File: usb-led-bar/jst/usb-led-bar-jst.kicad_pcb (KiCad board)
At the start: 2 copper layers, 100 x 15 mm, 18 parts, among them J1 JST PH 2-pin

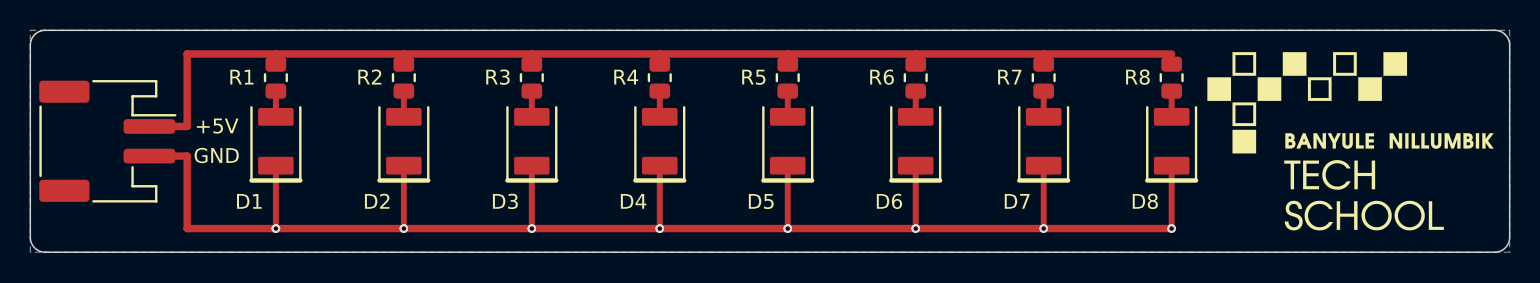
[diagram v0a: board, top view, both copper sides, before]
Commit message: Blank underside and M3 mounting hole at the logo end (both variants)
- Remove all back-side silkscreen (title, specs, JLC order-number marker);
  README now says to pick "Remove Mark" when ordering
- Add an M3 hole (3.2 mm NPTH, 6.9 mm head/washer keep-out) between D8
  and the logo; LED pitch 8.65 -> 7.65 mm to make room
- Regenerated schematics, boards (DRC clean, nets match), JLCPCB
  Gerber/BOM/CPL, previews and the USB-C STEP model; make_3d.py skips
  mounting-hole footprints

Co-Authored-By: Claude Opus 5.5 <noreply@anthropic.com>
Claude-Session: https://claude.ai/code/session_013C9F11DiXqXJzCTtebCnow
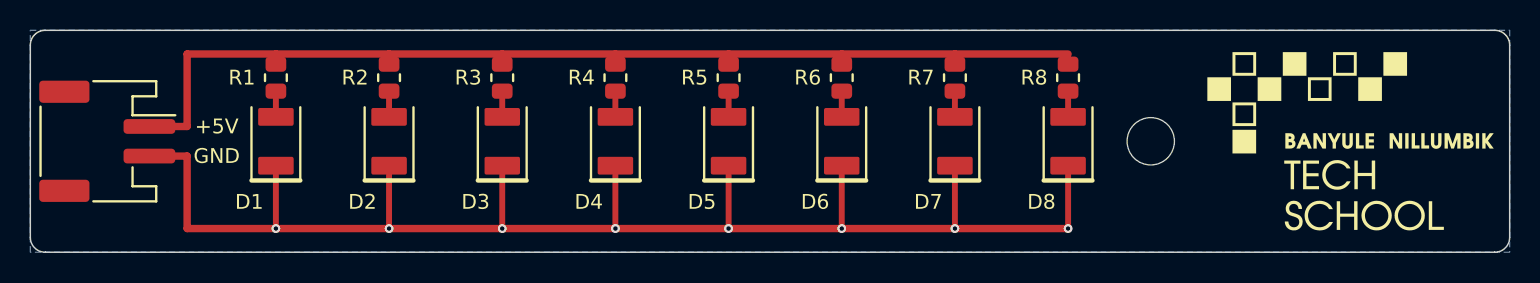
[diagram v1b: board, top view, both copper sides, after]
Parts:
- added H1: M3, MountingHole:MountingHole_3.2mm_M3, F.Cu at (175.7, 107.5)
- moved D8 7.00 mm to (170.2, 107.5)
- moved R8 7.00 mm to (170.2, 103.2)
- moved D7 6.00 mm to (162.5, 107.5)
- moved R7 6.00 mm to (162.5, 103.2)
- moved D6 5.00 mm to (154.8, 107.5)
- moved R6 5.00 mm to (154.8, 103.2)
- moved D5 4.00 mm to (147.2, 107.5)
- moved R5 4.00 mm to (147.2, 103.2)
- moved D4 3.00 mm to (139.6, 107.5)
- moved R4 3.00 mm to (139.6, 103.2)
- moved D3 2.00 mm to (131.9, 107.5)
- moved R3 2.00 mm to (131.9, 103.2)
- moved D2 1.00 mm to (124.2, 107.5)
- moved R2 1.00 mm to (124.2, 103.2)
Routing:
- net GND: track 108.0 -> 101.0 mm
- net +5V: track 79.5 -> 72.5 mm
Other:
- board text removed: "8x WARM WHITE 2835 LED - 5V ~168mA"
- board text removed: "J1: JST PH 2.0 pin 1 = +5V pin 2 = GND"
- board text removed: "JLCJLCJLCJLC"
- board text removed: "USB LED BAR v2.0"
